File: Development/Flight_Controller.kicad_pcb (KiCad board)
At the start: 2 copper layers, 2 parts, among them U1 STM32F765IIT6

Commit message: + New Footprints, Started PCB
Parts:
- added C1, C10, C11, C14, C2, C26, C28, C29, C3, C31, C32, C33, C34, C37, C38, C39, C4, C40, C41, C46, C47, C48, C5, C62, C63, C64, C65, C66, C67, C68, C69, C70, C71, C74, C75, C76: 100nF, Capacitor_SMD:C_0402_1005Metric, F.Cu at (142.2, 99.8)
- added C12, C13, C18, C19, C20, C21, C22, C23, C24, C25, C7, C78, C8, C9: 47uF, Capacitor_SMD:C_0402_1005Metric, F.Cu at (142.2, 99.8)
- added C15, C30, C49, C50: 2.2uF, Capacitor_SMD:C_0402_1005Metric, F.Cu at (142.2, 99.8)
- added C16: 0.1uF, Capacitor_SMD:C_0402_1005Metric, F.Cu at (142.2, 99.8)
- added C17: 220nF, Capacitor_SMD:C_0402_1005Metric, F.Cu at (142.2, 99.8)
- added C27: 4.7uF, Capacitor_SMD:C_0402_1005Metric, F.Cu at (142.2, 99.8)
- added C35, C36: 27pF, Capacitor_SMD:C_0402_1005Metric, F.Cu at (142.2, 99.8)
- added C56, C57: 12pF, Capacitor_SMD:C_0402_1005Metric, F.Cu at (142.2, 99.8)
- added C6: 470nF, Capacitor_SMD:C_0402_1005Metric, F.Cu at (142.2, 99.8)
- added C72, C73, C77, C79, C80, C81: 100nf, Capacitor_SMD:C_0402_1005Metric, F.Cu at (142.2, 99.8)
- added D1: 1N5822, Diode_THT:D_DO-201AD_P15.24mm_Horizontal, F.Cu at (142.2, 107.4)
- added D2: SMLVN6RGB, LED_SMD:LED_ROHM_SMLVN6, F.Cu at (142.2, 99.8)
- added J3: USB_C_Receptacle, Connector_USB:USB_C_Receptacle_Amphenol_12401610E4-2A_CircularHoles, F.Cu at (142.3, 99.8)
- added L1: L, Inductor_SMD:L_0402_1005Metric, F.Cu at (142.2, 99.8)
- added R10, R103, R3, R4, R74, R8: 1K, Resistor_SMD:R_0402_1005Metric, F.Cu at (142.2, 99.8)
- added R100, R101, R102, R61, R62, R63, R64, R95, R96, R97, R98, R99: 100R, Resistor_SMD:R_0402_1005Metric, F.Cu at (142.2, 99.8)
- added R11, R12, R14, R15, R2, R22, R23, R24, R26, R27, R29, R30, R31, R32, R35, R36, R37, R38, R39, R40, R41, R42, R43, R44, R45, R9: 10K, Resistor_SMD:R_0402_1005Metric, F.Cu at (142.2, 99.8)
- added R13: 50K, Resistor_SMD:R_0402_1005Metric, F.Cu at (142.2, 99.8)
- added R16: 1K5, Resistor_SMD:R_0402_1005Metric, F.Cu at (142.2, 99.8)
- added R17, R18, R20, R21, R48, R49, R50, R51, R52, R53, R54, R55, R70, R71, R72, R73, R77, R78, R79, R80, R87, R88, R89, R90: 100, Resistor_SMD:R_0402_1005Metric, F.Cu at (142.2, 99.8)
- added R19, R25, R6, R7: 0R, Resistor_SMD:R_0402_1005Metric, F.Cu at (142.2, 99.8)
- added R28: 1M, Resistor_SMD:R_0402_1005Metric, F.Cu at (142.2, 99.8)
- added R33, R34, R46, R47: 2M, Resistor_SMD:R_0402_1005Metric, F.Cu at (142.2, 99.8)
- added R5, R60, R65: 220R, Resistor_SMD:R_0402_1005Metric, F.Cu at (142.2, 99.8)
- added R56, R57, R58, R59, R75, R76: 10k, Resistor_SMD:R_0402_1005Metric, F.Cu at (142.2, 99.8)
- added R66, R67, R68, R69, R81, R82, R83, R84: 1k5, Resistor_SMD:R_0402_1005Metric, F.Cu at (142.2, 99.8)
- added R85, R91: 442K, Resistor_SMD:R_0402_1005Metric, F.Cu at (142.2, 99.8)
- added R86, R92: 24.9K, Resistor_SMD:R_0402_1005Metric, F.Cu at (142.2, 99.8)
- added R93, R94: 120, Resistor_SMD:R_0402_1005Metric, F.Cu at (142.2, 99.8)
- added U10: STM32F765IIT6, Package_QFP:LQFP-176_24x24mm_P0.5mm, F.Cu at (142.2, 99.8)
- added U12, U14, U18: TXS0108EPW, Package_SO:TSSOP-20_4.4x6.5mm_P0.65mm, F.Cu at (142.2, 99.8)
- added U15: FM25V02-G, FLIGHTFOOT:FM25V02-G, F.Cu at (142.2, 99.8)
- added U16, U17: TJA1051TK-3, Package_DFN_QFN:DFN-8-1EP_3x3mm_P0.65mm_EP1.55x2.4mm, F.Cu at (142.2, 99.8)
- added U2: ICM20689, FLIGHTFOOT:ICM20689, F.Cu at (142.2, 99.6)
- added U3, U4: MIC5330-SSYML, FLIGHTFOOT:MIC5330-SSYML-TR, F.Cu at (142.4, 99.7)
- added U5: MS5611-01BA, FLIGHTFOOT:ms5611, F.Cu at (142.2, 99.6)
- added U6: BMI088, FLIGHTFOOT:BMI088, F.Cu at (142.5, 99.8)
- added U7: IST8310, FLIGHTFOOT:ist8310, F.Cu at (142.2, 99.8)
- R1: value R -> 10K; footprint Resistor_SMD:R_0805_2012Metric_Pad1.15x1.40mm_HandSolder -> Resistor_SMD:R_0402_1005Metric
- U1: value STM32F765IIT6 -> MIC5330-SPYML; footprint Package_QFP:LQFP-176_24x24mm_P0.5mm -> FLIGHTFOOT:MIC5330-SSYML-TR
- moved R1 36.1 mm to (142.2, 99.8), turned to 270 degrees
- moved U1 15.7 mm to (142.4, 99.7), turned to 90 degrees
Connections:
- R1 pad 1: /SPI4_SCK_SENSOR2 -> GND
- R1 pad 2: GND -> SPI1_CS1_ICM20689
- U1 pad 1: /SPI4_SCK_SENSOR2 -> VCC
- U1 pad 2: Net-(U1-Pad2) -> GND
- U1 pad 4: Net-(U1-Pad4) -> VDD_3V3_SENSORS_EN
- U1 pad 5: Net-(U1-Pad5) -> VDD_3V3_SENSORS_EN
- U1 pad 7: Net-(U1-Pad7) -> IMU_VDD_3V0
- U1 pad 8: Net-(U1-Pad8) -> IMU_3V3
- U1 pad 9: Net-(U1-Pad9) -> (no net)

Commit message: PCB Started
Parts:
- added BT1: PAS414HR-VE5R, Newfootprint:UL_PAS414HRVE5R, F.Cu at (131.4, 26.7)
- added C42: 100nF, Capacitor_SMD:C_0402_1005Metric, F.Cu at (201.7, 84.6)
- added C43: 100nF, Capacitor_SMD:C_0402_1005Metric, F.Cu at (186.5, 99.6)
- added C44: DSM/SBUS RC, Connectors_JST:JST_GH_BM05B-GHS-TBT_05x1.25mm_Straight, F.Cu at (256.5, 76.2)
- added C45: GPS, Connectors_JST:JST_GH_BM10B-GHS-TBT_10x1.25mm_Straight, F.Cu at (237.5, 87.6)
- added C51: 2.2uF, Capacitor_SMD:C_0402_1005Metric, F.Cu at (156.8, 116.4)
- added C52: 2.2uF, Capacitor_SMD:C_0402_1005Metric, F.Cu at (192.4, 80.5)
- added C53: I2C3, Connectors_JST:JST_GH_BM04B-GHS-TBT_04x1.25mm_Straight, F.Cu at (255.9, 53.3)
- added C54: I2C4, Connectors_JST:JST_GH_BM04B-GHS-TBT_04x1.25mm_Straight, F.Cu at (255.9, 64.8)
- added C55: USART2, Connectors_JST:JST_GH_BM06B-GHS-TBT_06x1.25mm_Straight, F.Cu at (275.6, 41.9)
- added C58: 12pF, Capacitor_SMD:C_0402_1005Metric, F.Cu at (199.2, 73.2)
- added C59: 12pF, Capacitor_SMD:C_0402_1005Metric, F.Cu at (181.0, 89.6)
- added C60: SPI, Connectors_JST:JST_GH_BM07B-GHS-TBT_07x1.25mm_Straight, F.Cu at (275.0, 87.6)
- added C61: CAN1, Connectors_JST:JST_GH_BM04B-GHS-TBT_04x1.25mm_Straight, F.Cu at (233.7, 41.9)
- added C82: 100nf, Capacitor_SMD:C_0402_1005Metric, F.Cu at (202.6, 68.1)
- added C83: 100nf, Capacitor_SMD:C_0402_1005Metric, F.Cu at (192.4, 78.5)
- added D3: DIODE, LED_SMD:LED_0603_1608Metric, F.Cu at (106.4, 121.7)
- added D4: D240L, Diode_SMD:D_SOD-123, F.Cu at (101.4, 122.1)
- added J1: USB_C_Receptacle, Connector_USB:USB_C_Receptacle_Amphenol_12401610E4-2A_CircularHoles, F.Cu at (234.9, 25.4)
- added J2: Micro_SD_Card_Det, Connector_Card:microSD_HC_Hirose_DM3AT-SF-PEJM5, F.Cu at (103.5, 42.5)
- added J4: Conn_01x13_Female, Connector_PinHeader_2.54mm:PinHeader_1x13_P2.54mm_Vertical, F.Cu at (248.9, 25.4)
- added J5: Conn_01x13_Female, Connector_PinHeader_2.54mm:PinHeader_1x13_P2.54mm_Vertical, F.Cu at (248.9, 21.6)
- added LC1: EMI_Filter_LC, Newfootprint:CAP_NFM18PS105R0J3D, F.Cu at (157.9, 150.5)
- added LC10: EMI_Filter_LC, Newfootprint:CAP_NFM18PS105R0J3D, F.Cu at (142.5, 96.6)
- added LC11: EMI_Filter_LC, Newfootprint:CAP_NFM18PS105R0J3D, F.Cu at (146.4, 92.6)
- added LC12: EMI_Filter_LC, Newfootprint:CAP_NFM18PS105R0J3D, F.Cu at (134.6, 108.0)
- added LC13: EMI_Filter_LC, Newfootprint:CAP_NFM18PS105R0J3D, F.Cu at (145.7, 102.5)
- added LC14: EMI_Filter_LC, Newfootprint:CAP_NFM18PS105R0J3D, F.Cu at (152.4, 98.7)
- added LC15: EMI_Filter_LC, Newfootprint:CAP_NFM18PS105R0J3D, F.Cu at (152.4, 102.9)
- added LC16: EMI_Filter_LC, Newfootprint:CAP_NFM18PS105R0J3D, F.Cu at (128.3, 108.0)
- added LC2: EMI_Filter_LC, Newfootprint:CAP_NFM18PS105R0J3D, F.Cu at (146.1, 108.0)
- added LC3: EMI_Filter_LC, Newfootprint:CAP_NFM18PS105R0J3D, F.Cu at (146.4, 96.0)
- added LC4: EMI_Filter_LC, Newfootprint:CAP_NFM18PS105R0J3D, F.Cu at (137.2, 92.7)
- added LC5: EMI_Filter_LC, Newfootprint:CAP_NFM18PS105R0J3D, F.Cu at (129.5, 91.4)
- added LC6: EMI_Filter_LC, Newfootprint:CAP_NFM18PS105R0J3D, F.Cu at (141.0, 102.9)
- added LC7: EMI_Filter_LC, Newfootprint:CAP_NFM18PS105R0J3D, F.Cu at (130.8, 97.8)
- added LC8: EMI_Filter_LC, Newfootprint:CAP_NFM18PS105R0J3D, F.Cu at (128.3, 102.9)
- added LC9: EMI_Filter_LC, Newfootprint:CAP_NFM18PS105R0J3D, F.Cu at (134.6, 102.9)
- added U11: SN74LVC8T245, Newfootprint:SOP65P640X120-24N, F.Cu at (198.1, 29.2)
- added U13: NUF2042XV6T1G, Newfootprint:SOT50P160X60-6N, F.Cu at (121.6, 121.6)
- added U8: EG5350CT, Button_Switch_SMD:SW_SPST_EVQP7C, F.Cu at (204.5, 52.1)
- added U9: TPS3808, Newfootprint:SOT95P280X145-6N, F.Cu at (139.1, 120.7)
- added Y1: ABS06-32.768KHZ-9-T, Newfootprint:XTAL_ABS06-32.768KHZ-9-T, F.Cu at (110.5, 121.9)
- added Y2: Q22FA12800400, Newfootprint:Q22FA12800400, F.Cu at (117.6, 121.9)
- C35: value 27pF -> POWER1; footprint Capacitor_SMD:C_0402_1005Metric -> Connectors_JST:JST_GH_BM06B-GHS-TBT_06x1.25mm_Straight
- C36: value 27pF -> POWER2; footprint Capacitor_SMD:C_0402_1005Metric -> Connectors_JST:JST_GH_BM06B-GHS-TBT_06x1.25mm_Straight
- C37, C38: value 100nF -> 27pF
- C46: value 100nF -> ADC3/5; footprint Capacitor_SMD:C_0402_1005Metric -> Connectors_JST:JST_GH_BM04B-GHS-TBT_04x1.25mm_Straight
- C47: value 100nF -> DSU; footprint Capacitor_SMD:C_0402_1005Metric -> Connectors_JST:JST_GH_BM06B-GHS-TBT_06x1.25mm_Straight
- C49, C50: value 2.2uF -> 100nF
- C56: value 12pF -> USART3; footprint Capacitor_SMD:C_0402_1005Metric -> Connectors_JST:JST_GH_BM06B-GHS-TBT_06x1.25mm_Straight
- C57: value 12pF -> I2C2; footprint Capacitor_SMD:C_0402_1005Metric -> Connectors_JST:JST_GH_BM04B-GHS-TBT_04x1.25mm_Straight
- C62: value 100nF -> CAN2; footprint Capacitor_SMD:C_0402_1005Metric -> Connectors_JST:JST_GH_BM04B-GHS-TBT_04x1.25mm_Straight
- C63: value 100nF -> UART4; footprint Capacitor_SMD:C_0402_1005Metric -> Connectors_JST:JST_GH_BM06B-GHS-TBT_06x1.25mm_Straight
- C72, C73, C77: value 100nf -> 100nF
- C74, C75: value 100nF -> 100nf
- C78: value 47uF -> 100nF
- C80: value 100nf -> 47uF
- D1: value 1N5822 -> 1N4148WS; footprint Diode_THT:D_DO-201AD_P15.24mm_Horizontal -> Diode_SMD:D_SOD-323
- J3: value USB_C_Receptacle -> Conn_01x13_Female; footprint Connector_USB:USB_C_Receptacle_Amphenol_12401610E4-2A_CircularHoles -> Connector_PinHeader_2.54mm:PinHeader_1x13_P2.54mm_Vertical
- R56, R57, R58: value 10k -> 3k
- R59: value 10k -> 2k
- moved C56 141.2 mm to (275.6, 53.3), turned to 0 degrees
- moved C63 137.9 mm to (275.6, 64.8), turned to 0 degrees
- moved C47 135.4 mm to (275.6, 76.2), turned to 0 degrees
- moved J3 127.9 mm to (248.9, 29.2)
- moved C57 127.6 mm to (255.9, 41.9), turned to 0 degrees
- moved C35 115.6 mm to (257.2, 87.6), turned to 0 degrees
- moved C62 102.6 mm to (233.7, 53.3), turned to 0 degrees
- moved D2 99.3 mm to (212.1, 29.2), turned to 0 degrees
- moved C46 97.9 mm to (233.7, 64.8), turned to 0 degrees
- moved C36 95.7 mm to (234.9, 76.2), turned to 0 degrees
- moved U15 86.1 mm to (175.3, 20.3), turned to 0 degrees
- moved R67 83.1 mm to (141.0, 182.9)
- moved C31 78.8 mm to (141.0, 178.6)
- moved R3 75.0 mm to (141.0, 174.8)
- moved C64 73.5 mm to (205.7, 62.7), turned to 0 degrees
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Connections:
- C35 pad 1: /32KHz_OUT -> VCC
- C35 pad 2: GND -> VCC
- C36 pad 1: /32KHz_IN -> (no net)
- C36 pad 2: GND -> (no net)
- C37 pad 1: MCU_3V3 -> /32KHz_OUT
- C38 pad 1: MCU_3V3 -> /32KHz_IN
- C46 pad 1: MCU_3V3 -> Net-(C46-Pad1)
- C46 pad 2: GND -> ADC1_SPARE_1_CHANNEL
- C47 pad 1: MCU_3V3 -> Net-(C47-Pad1)
- C47 pad 2: GND -> UART7_TX
- C48 pad 1: NRST -> MCU_3V3
- C49 pad 1: Net-(C49-Pad1) -> MCU_3V3
- C50 pad 1: Net-(C50-Pad1) -> NRST
- C56 pad 1: /16_MHZ_OUT -> Net-(C56-Pad1)
- C56 pad 2: GND -> USART3_TX
- C57 pad 1: /16_MHZ_IN -> Net-(C57-Pad1)
- C57 pad 2: GND -> I2C_3_SCL_PORT
- C62 pad 1: TF_3V3 -> Net-(C62-Pad1)
- C62 pad 2: GND -> CAN_H_2
- C63 pad 1: SCALED_V5 -> Net-(C63-Pad1)
- C63 pad 2: GND -> UART4_TX
- C64 pad 1: GND -> TF_3V3
- C64 pad 2: BAT2_V -> GND
- C65 pad 1: GND -> SCALED_V5
- C65 pad 2: BAT2_I -> GND
- C66 pad 1: ADC1_SPARE_2 -> GND
- C66 pad 2: GND -> BAT2_V
- C67 pad 1: ADC1_SPARE_1 -> GND
- C67 pad 2: GND -> BAT2_I
- C68 pad 1: SCALED_VDD_3V3_SENSORS -> ADC1_SPARE_2
- C69 pad 1: GND -> ADC1_SPARE_1
- C69 pad 2: BAT1_V -> GND
- C70 pad 1: GND -> SCALED_VDD_3V3_SENSORS
- C70 pad 2: BAT1_I -> GND
- C71 pad 1: TF_3V3 -> GND
- C71 pad 2: GND -> BAT1_V
- C72 pad 2: IO1_3V3 -> BAT1_I
- C73 pad 1: GND -> TF_3V3
- C73 pad 2: D2_3V3 -> GND
- C74 pad 1: VCC -> GND
- C74 pad 2: GND -> IO1_3V3
- C75 pad 1: VCC -> GND
- C75 pad 2: GND -> D2_3V3
- C76 pad 1: GND -> VCC
- C76 pad 2: D2_3V3 -> GND
- C77 pad 1: GND -> VCC
- C77 pad 2: IO1_3V3 -> GND
- C78 pad 1: VCC -> GND
- C78 pad 2: GND -> D2_3V3
- C79 pad 2: D2_3V3 -> IO1_3V3
- C80 pad 1: GND -> VCC
- C80 pad 2: IO1_3V3 -> GND
- R10 pad 1: (no net) -> Net-(C35-Pad3)
- R100 pad 2: (no net) -> USART3_TX
- R101 pad 2: (no net) -> USART3_CTS
- R102 pad 2: (no net) -> USART3_RTS
- R11 pad 1: (no net) -> Net-(C36-Pad3)
- R12 pad 2: (no net) -> Net-(R12-Pad2)
- R13 pad 1: (no net) -> Net-(R13-Pad1)
- R17 pad 1: (no net) -> /SAFETY_IN
- R18 pad 1: (no net) -> /SAFETY_SWITCH_LED
- R20 pad 1: (no net) -> Net-(C44-Pad2)
- R21 pad 2: (no net) -> Net-(C44-Pad3)
- R41 pad 1: (no net) -> ADC1_SPARE_2_CHANNEL
- R42 pad 1: (no net) -> ADC1_SPARE_1_CHANNEL
- R48 pad 1: (no net) -> Net-(R48-Pad1)
- R48 pad 2: (no net) -> OUT8
- R49 pad 1: (no net) -> Net-(R49-Pad1)
- R49 pad 2: (no net) -> OUT7
- R50 pad 1: (no net) -> Net-(R50-Pad1)
- R50 pad 2: (no net) -> OUT6
- R51 pad 1: (no net) -> Net-(R51-Pad1)
- R51 pad 2: (no net) -> OUT5
- R52 pad 1: (no net) -> Net-(R52-Pad1)
- R52 pad 2: (no net) -> OUT4
- R53 pad 1: (no net) -> Net-(R53-Pad1)
- R53 pad 2: (no net) -> OUT3
- R54 pad 1: (no net) -> Net-(R54-Pad1)
- R54 pad 2: (no net) -> OUT2
- R55 pad 1: (no net) -> Net-(R55-Pad1)
- R55 pad 2: (no net) -> OUT1
- R59 pad 1: (no net) -> Net-(D3-Pad2)
- R60 pad 1: (no net) -> RC_IN_PORT
- R61 pad 2: (no net) -> GPS1_RX1
- R62 pad 2: (no net) -> GPS1_TX1
- R63 pad 2: (no net) -> UART4_TX
- R64 pad 2: (no net) -> UART4_RX
- R70 pad 1: (no net) -> I2C_3_SCL_PORT
- R71 pad 1: (no net) -> I2C_3_SDA_PORT
- R72 pad 1: (no net) -> SCL1_GPS
- R73 pad 1: (no net) -> SDA1_GPS
- R77 pad 2: (no net) -> AUX4
- R78 pad 2: (no net) -> AUX3
- R79 pad 2: (no net) -> AUX2
- R8 pad 1: (no net) -> Net-(C35-Pad4)
- R80 pad 2: (no net) -> AUX1
- R87 pad 1: (no net) -> I2C_4_SCL_PORT
- R88 pad 1: (no net) -> I2C_4_SDA_PORT
- R89 pad 1: (no net) -> I2C_2_SCL_PORT
- R9 pad 1: (no net) -> Net-(C36-Pad4)
- R90 pad 1: (no net) -> I2C_2_SDA_PORT
- R95 pad 2: (no net) -> USART2_RX
- R96 pad 2: (no net) -> USART2_TX
- R97 pad 2: (no net) -> USART2_RTS
- R98 pad 2: (no net) -> USART2_CTS
- R99 pad 2: (no net) -> USART3_RX
- U1 pad 6: Net-(U1-Pad6) -> (no net)
- U10 pad 101: (no net) -> FMU_CH5
- U10 pad 104: (no net) -> FMU_CH6
- U10 pad 12: (no net) -> SPI5_CS2_EXTERNAL1
- U10 pad 121: (no net) -> FMU_CH2
- U10 pad 122: (no net) -> OTG_FS_DM
- U10 pad 123: (no net) -> OTG_FS_DP
- U10 pad 124: (no net) -> JTAG_SWDIO
- U10 pad 125: Net-(C49-Pad1) -> Net-(C51-Pad1)
- U10 pad 137: (no net) -> JTAG_SWCLK
- U10 pad 141: (no net) -> SDMMC1_CLK
- U10 pad 173: (no net) -> SPI5_CS1_EXTERNAL1
- U10 pad 25: (no net) -> SPI5_SCK_EXTERNAL1
- U10 pad 26: (no net) -> SPI5_MISO_EXTERNAL1
- U10 pad 27: (no net) -> SPI5_MOSI_EXTERNAL1
- U10 pad 4: (no net) -> BUZZER_1
- U10 pad 70: (no net) -> FMU_CH4
- U10 pad 74: (no net) -> FMU_CH3
- U10 pad 77: (no net) -> FMU_CH1
- U10 pad 81: Net-(C50-Pad1) -> Net-(C52-Pad1)
- U10 pad 83: (no net) -> FMU_CH7
- U10 pad 86: (no net) -> FMU_CH8
- U12 pad 18: (no net) -> UART7_RX
- U12 pad 20: (no net) -> UART7_TX
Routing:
- net GND: track 0.00 -> 30.5 mm
- net Net-(J4-Pad1): track 0.00 -> 20.3 mm
- net Net-(J4-Pad10): track 0.00 -> 7.62 mm

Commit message: PCB layout editting
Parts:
- moved R10 145.3 mm to (294.0, 82.5)
- moved C39 144.3 mm to (69.8, 27.9), turned to 90 degrees
- moved R9 143.8 mm to (301.0, 87.6)
- moved C40 136.7 mm to (73.7, 27.9), turned to 90 degrees
- moved C42 133.1 mm to (81.3, 27.9), turned to 90 degrees
- moved C41 127.8 mm to (77.5, 27.9), turned to 90 degrees
- moved R11 127.3 mm to (301.0, 83.2)
- moved C43 124.2 mm to (85.1, 27.9), turned to 90 degrees
- moved C48 113.3 mm to (88.9, 27.9), turned to 90 degrees
- moved C24 112.1 mm to (154.9, 17.1)
- moved C20 111.6 mm to (149.2, 41.3), turned to 180 degrees
- moved C49 108.9 mm to (92.7, 27.9), turned to 90 degrees
- moved U16 108.6 mm to (49.5, 67.3)
- moved C7 108.6 mm to (130.2, 13.3)
- moved C13 103.0 mm to (146.1, 14.6)
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
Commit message: PCB Routing Update
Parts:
- C32, C37, C38, C39, C40, C41, C42, C43, C48, C49, C50, C51, C52, C58, C59, C79, C81, C82, C83, R100, R101, R102, R103, R14, R15, R19, R22, R23, R24, R25, R26, R27, R28, R29, R30, R6, R95, R96, R97, R98, R99, U10, U11, U14, U15, U18, Y1, Y2: moved to B.Cu
- C47: value DSU -> DSU7
- C60: value SPI -> SPI5
- moved R11 202.2 mm to (100.1, 105.7), turned to 270 degrees
- moved R9 200.7 mm to (101.1, 105.6), turned to 270 degrees
- moved R10 175.1 mm to (122.4, 117.3), turned to 270 degrees
- moved R8 172.7 mm to (124.0, 117.4), turned to 270 degrees
- moved R40 169.7 mm to (47.2, 135.1), turned to 180 degrees
- moved R42 166.9 mm to (37.6, 109.2), turned to 180 degrees
- moved R47 165.7 mm to (23.3, 114.8), turned to 180 degrees
- moved C74 155.5 mm to (119.9, 145.8), turned to 90 degrees
- moved R39 154.0 mm to (37.6, 110.2)
- moved R91 153.1 mm to (40.2, 95.5)
- moved U12 151.9 mm to (124.5, 142.2)
- moved J2 147.8 mm to (157.0, 134.6), turned to 90 degrees
- moved C67 146.6 mm to (23.4, 116.8)
- moved C75 144.1 mm to (129.6, 139.7), turned to 180 degrees
- moved C76 139.7 mm to (50.8, 97.5)
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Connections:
- Y2 pad 1: /16_MHZ_IN -> /16_MHZ_OUT
- Y2 pad 2: /16_MHZ_OUT -> GND
- Y2 pad 3: (no net) -> /16_MHZ_IN
- Y2 pad 4: (no net) -> GND
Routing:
- net FMU_CAP1: track 0.00 -> 58.2 mm
- net Net-(R80-Pad1): track 0.00 -> 54.0 mm, vias 0 -> 1
- net Net-(R79-Pad1): track 0.00 -> 54.0 mm, vias 0 -> 1
- net Net-(R78-Pad1): track 0.00 -> 53.9 mm, vias 0 -> 1
- net Net-(R77-Pad1): track 0.00 -> 53.9 mm, vias 0 -> 1
- net FMU_CAP2: track 0.00 -> 49.6 mm, vias 0 -> 2
- net FMU_CAP3: track 0.00 -> 45.9 mm
- net SPI2_CS_FRAM: track 0.00 -> 42.6 mm
- net GND: track 30.5 -> 62.5 mm
- net MCU_3V3: track 0.00 -> 30.8 mm
- net D2_3V3: track 0.00 -> 28.4 mm
- net TIM5_SPARE_4: track 0.00 -> 19.5 mm
- net OTG_N: track 0.00 -> 16.5 mm
- net USB_VCC: track 0.00 -> 16.1 mm
- net VCC: track 0.00 -> 13.7 mm
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
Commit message: PCB Routing 27 Sep
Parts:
- BT1, C33, C78, R40, R7: moved to B.Cu
- moved C3 123.9 mm to (131.1, 130.6)
- moved C9 123.9 mm to (130.0, 128.5)
- moved C12 123.9 mm to (131.1, 128.5)
- moved U1 123.9 mm to (133.1, 130.3)
- moved C13 122.2 mm to (112.8, 128.5)
- moved C2 121.8 mm to (120.9, 130.0)
- moved U3 121.8 mm to (122.9, 129.9)
- moved C8 121.8 mm to (120.9, 128.0)
- moved C18 120.8 mm to (112.8, 127.5), turned to 180 degrees
- moved C10 119.3 mm to (107.2, 128.5)
- moved C4 119.3 mm to (107.7, 130.0)
- moved C7 119.3 mm to (108.2, 128.5)
- moved R2 119.3 mm to (111.7, 131.6)
- moved U4 119.3 mm to (110.2, 129.5)
- moved C11 118.1 mm to (119.9, 128.0), turned to 270 degrees
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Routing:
- net GND: track 62.5 -> 143.3 mm, vias 0 -> 10
- net nLED_BLUE: track 0.00 -> 73.8 mm, vias 0 -> 1
- net nLED_RED: track 0.00 -> 53.9 mm, vias 0 -> 3
- net USART2_RTS: track 0.00 -> 40.0 mm, vias 0 -> 1
- net USART2_RX: track 0.19 -> 34.4 mm, vias 0 -> 1
- net USART2_TX: track 0.14 -> 27.4 mm, vias 0 -> 1
- net USART2_CTS: track 0.19 -> 23.8 mm, vias 0 -> 1
- net SPI5_MOSI_EXTERNAL1: track 0.00 -> 22.1 mm, vias 0 -> 1
- net MCU_3V3: track 30.8 -> 50.9 mm
- net SPI4_CS1_MS5611: track 0.00 -> 19.8 mm, vias 0 -> 1
- net USART3_RX: track 0.00 -> 17.0 mm, vias 0 -> 1
- net USART3_TX: track 0.00 -> 13.6 mm, vias 0 -> 1
- net CAN_L_2: track 0.00 -> 13.6 mm
- net SCALED_V5: track 0.00 -> 13.6 mm, vias 0 -> 2
- net VCC: track 13.7 -> 27.2 mm
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- added copper zone on B.Cu, net GND
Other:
- board outline added: 84.8 x 118.9 mm

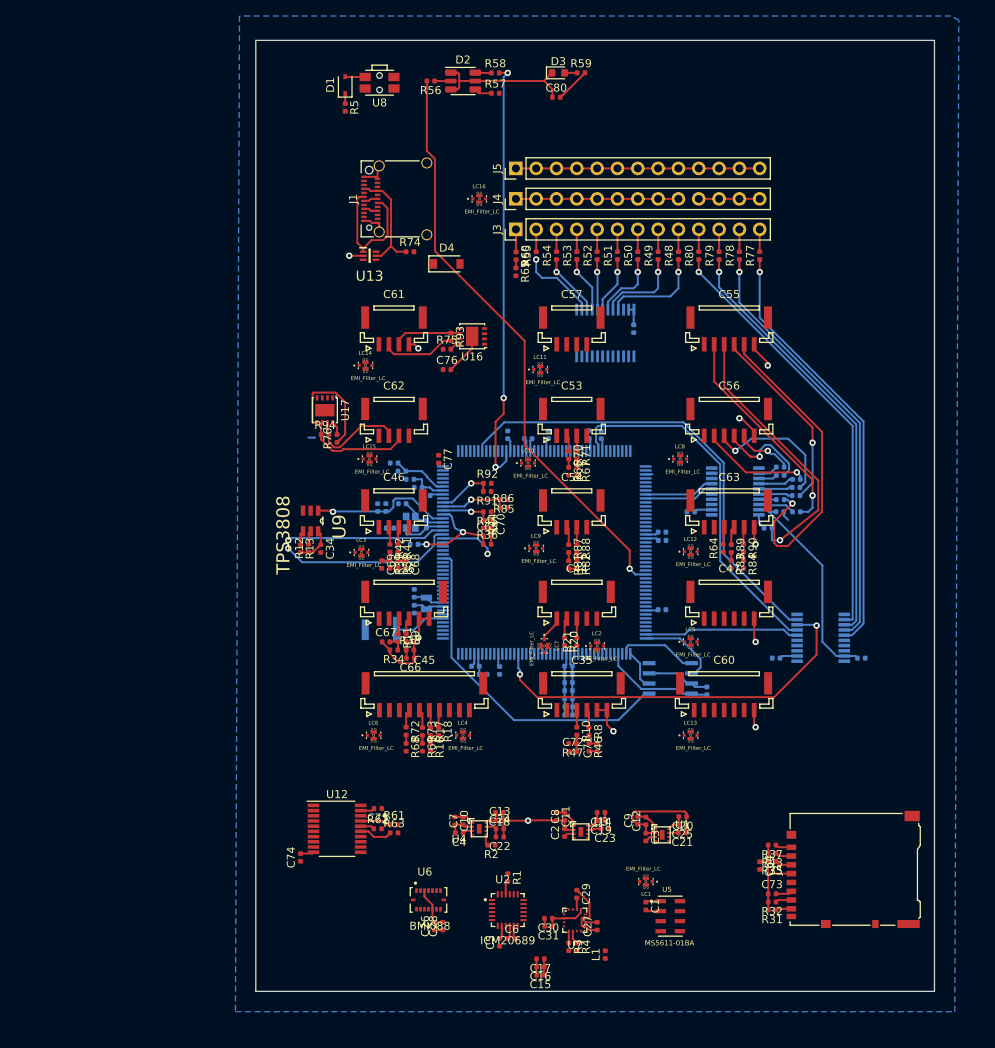
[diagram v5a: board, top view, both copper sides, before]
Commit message: PCB 4 layers, 89 unrouted
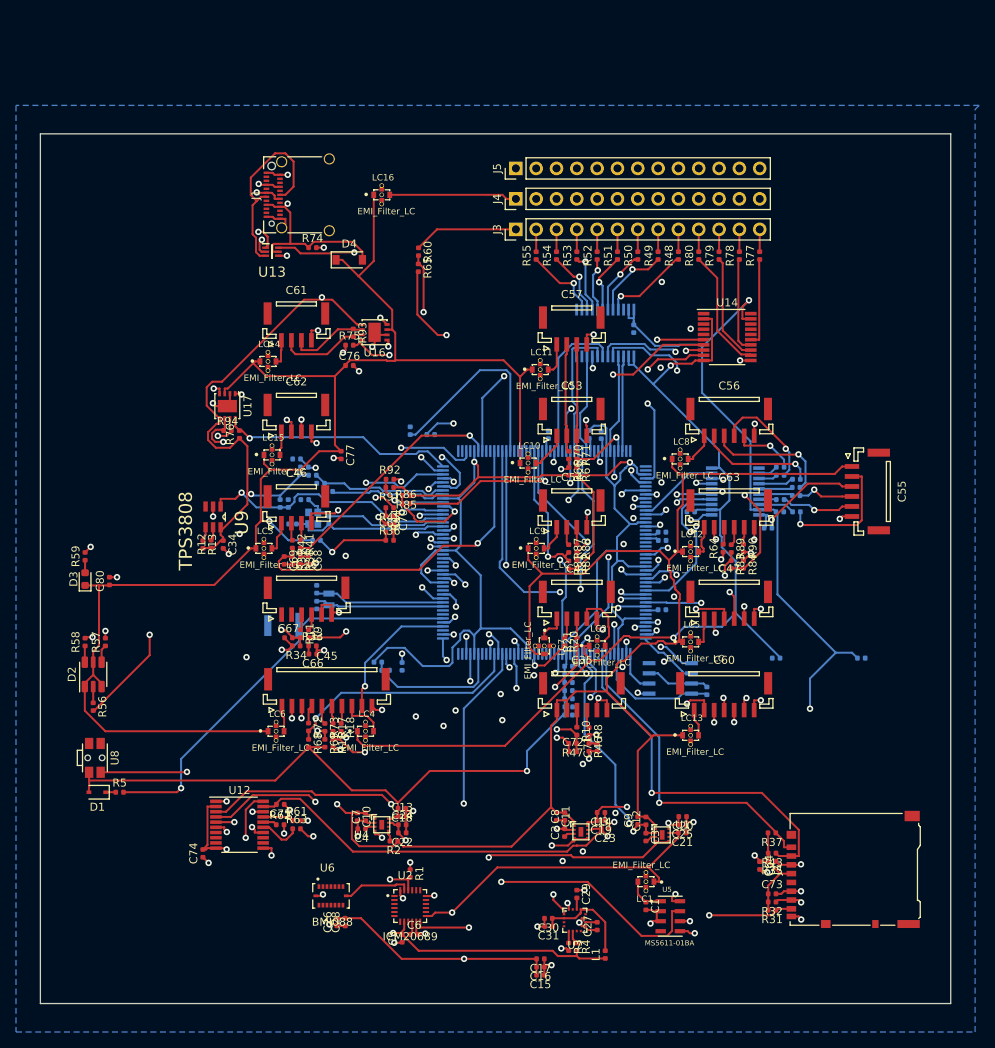
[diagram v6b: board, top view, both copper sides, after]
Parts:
- LC1, LC10, LC11, LC12, LC13, LC14, LC15, LC16, LC2, LC3, LC4, LC5, LC6, LC7, LC8, LC9: footprint Newfootprint:CAP_NFM18PS105R0J3D -> FLIGHTFOOT:FIL_NFM21PC105B1C3D
- U14: moved to F.Cu
- moved D1 93.7 mm to (62.5, 125.0), turned to 180 degrees
- moved U8 91.6 mm to (62.2, 120.7), turned to 270 degrees
- moved R5 90.1 mm to (65.3, 125.0), turned to 0 degrees
- moved R56 88.9 mm to (62.0, 114.3), turned to 270 degrees
- moved R58 87.7 mm to (61.0, 106.2), turned to 90 degrees
- moved D2 87.4 mm to (62.0, 110.2), turned to 90 degrees
- moved D3 86.6 mm to (61.0, 98.3), turned to 90 degrees
- moved R59 86.6 mm to (61.0, 95.5), turned to 90 degrees
- moved R57 84.2 mm to (63.5, 106.2), turned to 90 degrees
- moved C80 82.3 mm to (64.0, 98.6), turned to 90 degrees
- moved U14 39.4 mm to (141.2, 68.1)
- moved C55 26.3 mm to (158.5, 87.4), turned to 270 degrees
- moved U16 12.2 mm to (97.1, 67.5)
- moved BT1 12.2 mm to (85.3, 104.1)
- moved C10 12.2 mm to (95.0, 128.0)
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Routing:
- net MCU_3V3: track 50.9 -> 456.8 mm, vias 0 -> 10
- net VCC: track 27.2 -> 409.5 mm, vias 0 -> 2
- net IO1_3V3: track 8.66 -> 218.0 mm, vias 0 -> 4
- net D2_3V3: track 32.7 -> 165.6 mm, vias 0 -> 3
- net IMU_3V3: track 4.15 -> 131.7 mm, vias 0 -> 3
- net OTG_FS_DP: track 0.00 -> 97.3 mm, vias 0 -> 3
- net UART4_TX: track 0.14 -> 91.0 mm, vias 0 -> 3
- net VBUS: track 0.00 -> 89.9 mm, vias 0 -> 3
- net UART7_TX: track 0.00 -> 89.6 mm, vias 0 -> 2
- net Net-(R64-Pad1): track 0.00 -> 89.6 mm, vias 0 -> 3
- net SPI1_DRDY3_BMI055_ACC: track 0.00 -> 87.2 mm, vias 0 -> 3
- net UART7_TX_DEBUG: track 0.00 -> 80.6 mm, vias 0 -> 3
- net nLED_GREEN: track 0.00 -> 77.6 mm, vias 0 -> 2
- net SPI4_MISO_SENSOR2: track 0.00 -> 77.1 mm, vias 0 -> 2
- net VDD_3V3_SD_CARD_EN: track 0.00 -> 75.2 mm, vias 0 -> 3
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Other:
- board size 84.8 x 118.9 mm -> 113.8 x 108.7 mm
- copper layers 2 -> 4

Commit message: Completed all PCB connections
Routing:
- net GND: track 134.3 -> 526.6 mm, vias 56 -> 91
- net SPI1_MISO_SENSOR1: track 0.00 -> 90.7 mm, vias 0 -> 6
- net SPI1_DRDY6_BMI055_ACC: track 0.00 -> 87.1 mm, vias 0 -> 8
- net SPI1_DRDY2_BMI055_GYRO: track 0.00 -> 84.2 mm, vias 0 -> 7
- net UART4_RX_I2C2: track 0.00 -> 82.2 mm, vias 0 -> 3
- net SPI1_CS4_BMI055_ACC: track 0.00 -> 65.1 mm, vias 0 -> 2
- net SPI1_DRDY5_BMI055_GYRO: track 0.00 -> 54.6 mm, vias 0 -> 3
- net SPI1_CS3_BMI055_GYRO: track 0.00 -> 48.2 mm, vias 0 -> 4
- net SPI1_SCK_SENSOR1: track 8.55 -> 52.3 mm, vias 0 -> 3
- net SDMMC1_CLK: track 0.00 -> 42.9 mm, vias 0 -> 3
- net MCU_3V3: track 456.8 -> 476.8 mm, vias 10 -> 11
- net /nVDD_5V_HIPOWER_OC: track 0.00 -> 14.6 mm, vias 0 -> 2
- net SPI1_MOSI_SENSOR1: track 50.1 -> 58.3 mm
- net VCC: track 409.5 -> 416.9 mm
- net SPI1_DRDY3_BMI055_ACC: track 87.2 -> 93.8 mm
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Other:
- rule trace_min: 0.2 -> 0.1
- rule via_min_size: 0.4 -> 0.1

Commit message: Shrunt PCB size to 100x100mm
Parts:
- moved R56 14.4 mm to (76.4, 115.3)
- moved D2 14.4 mm to (76.4, 110.6)
- moved R58 14.0 mm to (75.0, 106.4)
- moved R57 13.3 mm to (76.8, 106.0)
- moved U8 13.2 mm to (75.3, 119.6)
- moved D3 12.4 mm to (72.8, 101.8)
- moved R59 12.4 mm to (72.8, 98.9)
- moved C80 12.4 mm to (75.9, 102.0)
- moved D1 9.87 mm to (72.2, 123.3), turned to 90 degrees
- moved R5 9.19 mm to (74.4, 124.3)
- moved C15 5.72 mm to (114.1, 143.5)
- moved C16 5.72 mm to (114.1, 142.5)
- moved C17 5.72 mm to (114.1, 141.5)
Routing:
- net VCC: track 416.9 -> 392.6 mm
- net nLED_GREEN: track 77.7 -> 64.5 mm
- net BOOT0: track 62.3 -> 49.7 mm
- net nLED_RED: track 71.5 -> 59.5 mm
- net MCU_3V3: track 476.8 -> 465.3 mm
- net nLED_BLUE: track 79.6 -> 68.8 mm
- net VBAT: track 52.4 -> 45.3 mm
- net IMU_VDD_3V0: track 80.3 -> 78.1 mm, vias 2 -> 3
- net Net-(D2-Pad2): track 2.03 -> 2.71 mm
- net Net-(D2-Pad4): track 2.23 -> 2.84 mm
- net Net-(D1-Pad1): track 1.26 -> 1.77 mm
- removed copper zone on B.Cu, net GND
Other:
- board size 113.8 x 108.7 mm -> 98.7 x 104 mm
